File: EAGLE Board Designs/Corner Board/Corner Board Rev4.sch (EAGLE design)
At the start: 63 parts, among them J1 CONNECTOR-8_AMPHENOL_M12A_08P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, J2 CONNECTOR-2_MICROFIT_SMD_RIGH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, J3 BINDER-M12-A_4_PIN, J4 CONNECTOR-4_μF_S_RA_, T1 78613/3C_78613/3C_AIRGAP, U1 MAX7404, U10 LTC6820, U11 MCP3204, U2 OPAMP_1_CHANNEL_OPA991, U3 INA823DT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

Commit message: fixed voltage divider gain text
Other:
- note added: "0.666x gain"
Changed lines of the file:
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@@
 <wire x1="271.018" y1="207.772" x2="145.034" y2="208.026" width="0.1524" layer="97"/>
 <text x="147.828" y="203.962" size="1.778" layer="97" font="vector">RAE Tech SteeringTorque Sensor</text>
+<text x="187.198" y="168.402" size="1.27" layer="97" font="vector">0.666x gain</text>
 </plain>
 <instances>

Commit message: eagle is delayed
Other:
- note added: "0.67x gain"
- note removed: "0.666x gain"
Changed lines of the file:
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@@
 <wire x1="271.018" y1="207.772" x2="145.034" y2="208.026" width="0.1524" layer="97"/>
 <text x="147.828" y="203.962" size="1.778" layer="97" font="vector">RAE Tech SteeringTorque Sensor</text>
-<text x="187.198" y="168.402" size="1.27" layer="97" font="vector">0.666x gain</text>
+<text x="187.198" y="168.402" size="1.27" layer="97" font="vector">0.67x gain</text>
 </plain>
 <instances>

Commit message: small changes
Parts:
- added J5: CONNECTOR-4_μF_S_RA_, HyTechDevices:CONNECTOR-4_μF_S_RA_
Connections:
- net +24V: now also J5.1
- net GND: now also J5.4
- net STEER_TORQUE_24V: now also J5.3
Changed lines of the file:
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@@
 <part name="R7" library="HyTechDevices" deviceset="RESISTOR_?_*" device="0603" technology="10K"/>
 <part name="R8" library="HyTechDevices" deviceset="RESISTOR_?_*" device="0603" technology="20K"/>
+<part name="J5" library="HyTechDevices" deviceset="CONNECTOR-4_?_*" device="μF_S_RA" value="CONNECTOR-4_μF_S_RA_"/>
+<part name="P63" library="HyTechSupplies" deviceset="GND" device=""/>
+<part name="U$8" library="HyTechSupplies" deviceset="+24V" device=""/>
 </parts>
 <sheets>
@@
 <attribute name="VALUE" x="201.93" y="71.628" size="1.27" layer="96" align="bottom-center"/>
 </instance>
+<instance part="J5" gate="G$1" x="5.08" y="-42.418" smashed="yes">
+<attribute name="MPN" x="5.08" y="-55.753" size="1.27" layer="96" align="top-left"/>
+<attribute name="NAME" x="5.08" y="-41.656" size="1.27" layer="95"/>
+</instance>
+<instance part="P63" gate="1" x="17.78" y="-57.658" smashed="yes">
+<attribute name="VALUE" x="17.78" y="-58.928" size="1.27" layer="96" align="top-center"/>
+</instance>
+<instance part="U$8" gate="G$1" x="17.78" y="-39.878" smashed="yes">
+<attribute name="VALUE" x="17.78" y="-34.798" size="1.778" layer="96" align="bottom-center"/>
+</instance>
 </instances>
 <busses>
@@
 <pinref part="P12" gate="1" pin="GND"/>
 </segment>
+<segment>
+<pinref part="J5" gate="G$1" pin="4"/>
+<pinref part="P63" gate="1" pin="GND"/>
+<wire x1="15.24" y1="-52.578" x2="17.78" y2="-52.578" width="0.1524" layer="91"/>
+<wire x1="17.78" y1="-52.578" x2="17.78" y2="-55.118" width="0.1524" layer="91"/>
+</segment>
 </net>
 <net name="SIGNAL_P" class="0">
@@
 <junction x="73.66" y="63.5"/>
 </segment>
+<segment>
+<pinref part="U$8" gate="G$1" pin="+24V"/>
+<wire x1="17.78" y1="-44.958" x2="17.78" y2="-42.418" width="0.1524" layer="91"/>
+<pinref part="J5" gate="G$1" pin="1"/>
+<wire x1="17.78" y1="-44.958" x2="15.24" y2="-44.958" width="0.1524" layer="91"/>
+</segment>
 </net>
 <net name="SUS_POT_1" class="0">
@@
 </segment>
 </net>
+<net name="STEER_TORQUE_24V" class="0">
+<segment>
+<pinref part="J5" gate="G$1" pin="3"/>
+<wire x1="15.24" y1="-50.038" x2="18.288" y2="-50.038" width="0.1524" layer="91"/>
+<label x="18.288" y="-50.038" size="1.27" layer="95" font="vector" xref="yes"/>
+</segment>
+</net>

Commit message: did some routing
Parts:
- C2: value CAPACITOR_0603_25V_0.1UF -> CAPACITOR_0603_35V_0.1UF; device HyTechDevices:CAPACITOR_0603_25V_0.1UF -> HyTechDevices:CAPACITOR_0603_35V_0.1UF
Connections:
- net +24V: now also C2.1, U3P.VDD
- net +3V3: no longer C2.1, U3P.VDD
- net LOAD_CELL_FILTERED: now also U11.CH2; no longer U11.CH0
- net STEER_TORQUE_FILTERED: now also U11.CH0
- net SUS_POT_FILTERED: now also U11.CH1; no longer U11.CH2
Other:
- moved on the sheet: U11

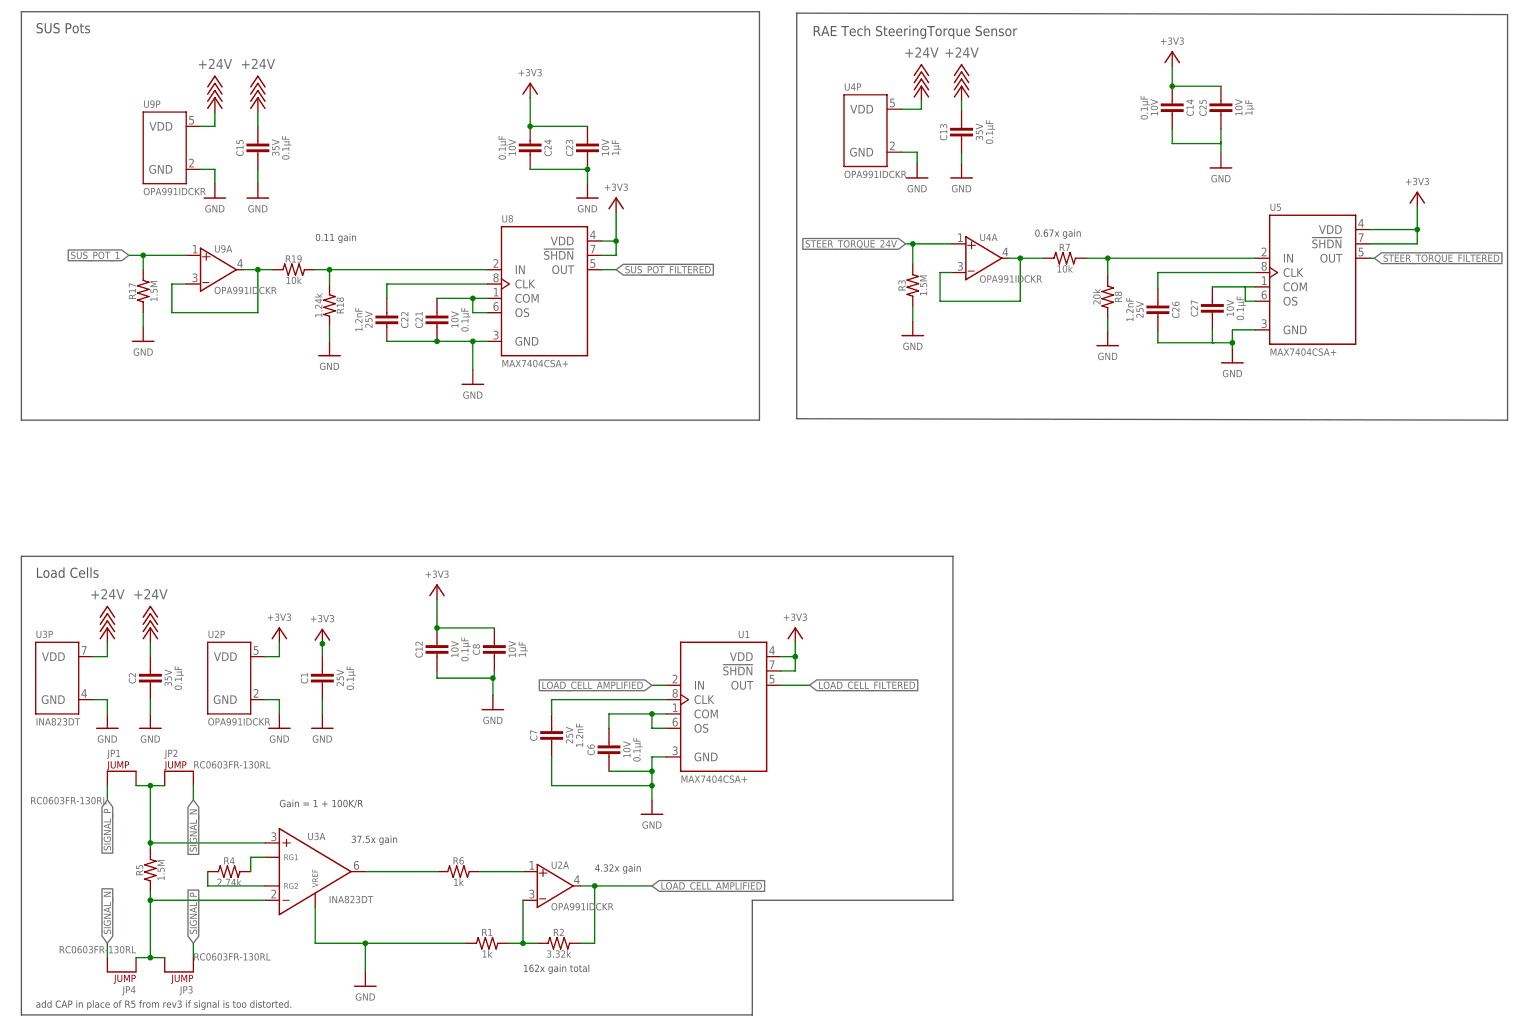
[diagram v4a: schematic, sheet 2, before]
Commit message: changed non crit for 2nd order
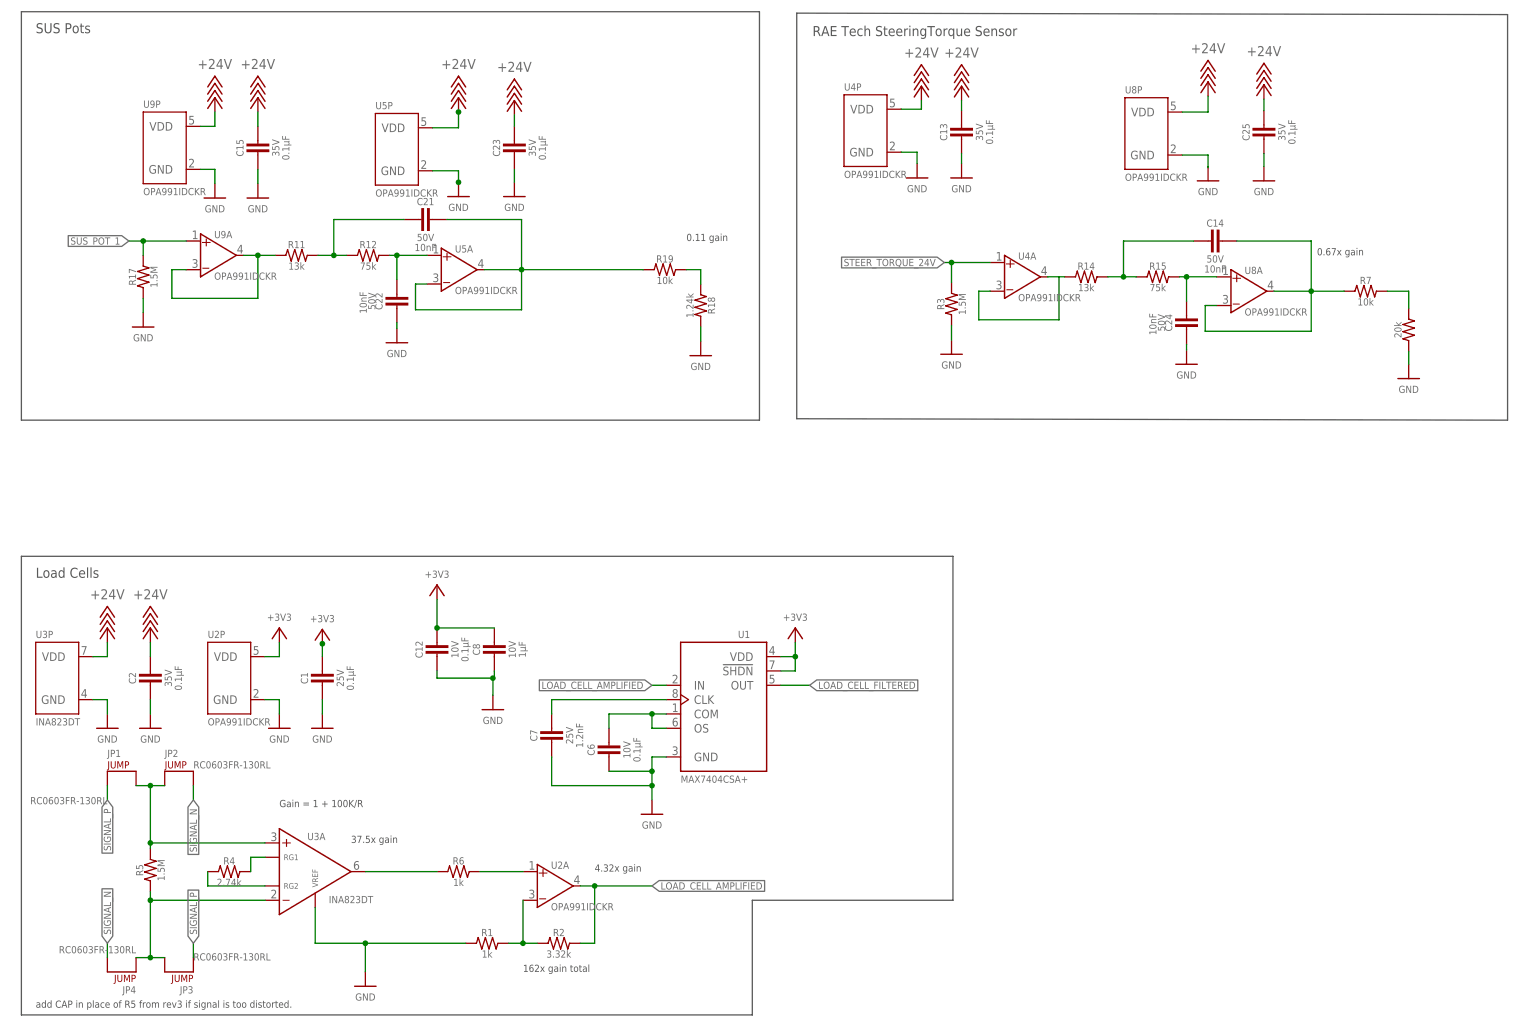
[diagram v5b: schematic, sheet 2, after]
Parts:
- removed C26: CAPACITOR_0603_25V_1.2NF, HyTechDevices:CAPACITOR_0603_25V_1.2NF
- removed C27: CAPACITOR_0603_10V_0.1UF, HyTechDevices:CAPACITOR_0603_10V_0.1UF
- added R11, R14: RESISTOR_0603_13K, HyTechDevices:RESISTOR_0603_13K
- added R12, R15: RESISTOR_0603_75K, HyTechDevices:RESISTOR_0603_75K
- C14, C21, C24: value CAPACITOR_0603_10V_0.1UF -> CAPACITOR_0603_50V_10NF; device HyTechDevices:CAPACITOR_0603_10V_0.1UF -> HyTechDevices:CAPACITOR_0603_50V_10NF
- C22: value CAPACITOR_0603_25V_1.2NF -> CAPACITOR_0603_50V_10NF; device HyTechDevices:CAPACITOR_0603_25V_1.2NF -> HyTechDevices:CAPACITOR_0603_50V_10NF
- C23, C25: value CAPACITOR_0603_10V_1UF -> CAPACITOR_0603_35V_0.1UF; device HyTechDevices:CAPACITOR_0603_10V_1UF -> HyTechDevices:CAPACITOR_0603_35V_0.1UF
- U5, U8: value MAX7404 -> OPAMP_1_CHANNEL_OPA991; device HyTechDevices:MAX7404 -> HyTechDevices:OPAMP_1_CHANNEL_OPA991
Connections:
- new net N$49: C22.1, R12.2, U5A.VIN+
- new net N$52: C24.1, R15.2, U8A.VIN+
- new net N$55: R7.1
- net +24V: now also C23.1, C25.1, U5P.VDD, U8P.VDD
- net +3V3: no longer C14.2, C23.1, C24.2, C25.1, U5.!SHDN, U5.VDD, U8.!SHDN, U8.VDD
- net GND: now also C22.2, C24.2, U5P.GND, U8P.GND; no longer C14.1, C21.2, C22.1, C24.1, C26.1, C27.2, U5.GND, U8.GND
- net N$15: now also C14.1, U8A.VIN-, U8A.VOUT; no longer C21.1, U8.COM, U8.OS
- net N$22: now also C21.1, R19.1, U5A.VIN-, U5A.VOUT; no longer C22.2, U8.CLK
- net N$51: now also R14.1; no longer R7.1
- net N$53: now also C21.2, R11.2, R12.1; no longer C27.1, U5.COM, U5.OS
- net N$54: now also C14.2, R14.2, R15.1; no longer C26.2, U5.CLK
- net STEER_TORQUE_3V3: no longer U5.IN
- net STEER_TORQUE_FILTERED: no longer U5.OUT
- net SUS_POT_1_24V1: now also R11.1; no longer R19.1
- net SUS_POT_1_3V3: no longer U8.IN
- net SUS_POT_FILTERED: no longer U8.OUT
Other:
- moved on the sheet: C14, C21, C22, C23, C24, C25, R17, R18, R19, R3, R7, U4A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

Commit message: redid everything
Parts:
- removed C13, C25: CAPACITOR_0603_35V_0.1UF, HyTechDevices:CAPACITOR_0603_35V_0.1UF
- removed C14, C24: CAPACITOR_0603_50V_10NF, HyTechDevices:CAPACITOR_0603_50V_10NF
- removed J5: CONNECTOR-4_μF_S_RA_, HyTechDevices:CONNECTOR-4_μF_S_RA_
- removed R14: RESISTOR_0603_13K, HyTechDevices:RESISTOR_0603_13K
- removed R15: RESISTOR_0603_75K, HyTechDevices:RESISTOR_0603_75K
- removed R3: RESISTOR_0603_1.5M, HyTechDevices:RESISTOR_0603_1.5M
- removed R7: RESISTOR_0603_10K, HyTechDevices:RESISTOR_0603_10K
- removed R8: RESISTOR_0603_20K, HyTechDevices:RESISTOR_0603_20K
- removed U4, U8: OPAMP_1_CHANNEL_OPA991, HyTechDevices:OPAMP_1_CHANNEL_OPA991
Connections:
- removed net N$15: C14.1, U8A.VIN-, U8A.VOUT
- removed net N$51: R14.1, U4A.VIN-, U4A.VOUT
- removed net N$52: C24.1, R15.2, U8A.VIN+
- removed net N$54: C14.2, R14.2, R15.1
- removed net N$55: R7.1
- removed net STEER_TORQUE_24V: J5.3, R3.2, U4A.VIN+
- removed net STEER_TORQUE_3V3: R7.2, R8.1
- removed net STEER_TORQUE_FILTERED: U11.CH0
- net +24V: no longer C13.1, C25.1, J5.1, U4P.VDD, U8P.VDD
- net DIFF_N: now also J1.6; no longer J1.4
- net DIFF_P: now also J1.5; no longer J1.3
- net GND: no longer C13.2, C24.2, C25.2, J5.4, R3.1, R8.2, U4P.GND, U8P.GND
- net POSTINTERLOCK: now also J1.4; no longer J1.6
- net PREINTERLOCK: now also J1.3; no longer J1.5
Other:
- note removed: "0.67x gain"
- note removed: "RAE Tech SteeringTorque Sensor"

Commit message: almost done
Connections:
- removed net SUS_POT_FILTERED: U11.CH1
- net SUS_POT_1_3V3: now also U11.CH1
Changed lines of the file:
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@@
 </segment>
 </net>
-<net name="SUS_POT_FILTERED" class="0">
+<net name="SUS_POT_1_3V3" class="0">
 <segment>
 <pinref part="U11" gate="G$1" pin="CH1"/>

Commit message: finito
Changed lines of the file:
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@@
-</segment>
-</net>
-<net name="LOAD_CELL_FILTERED" class="0">
-<segment>
-<pinref part="U1" gate="G$1" pin="OUT"/>
-<wire x1="142.24" y1="88.9" x2="147.32" y2="88.9" width="0.1524" layer="91"/>
-<label x="147.32" y="88.9" size="1.27" layer="95" font="vector" xref="yes"/>
 </segment>
 </net>
@@
 </segment>
 </net>
+<net name="LOAD_CELL_FILTERED" class="0">
+<segment>
+<pinref part="U1" gate="G$1" pin="OUT"/>
+<wire x1="142.24" y1="88.9" x2="145.034" y2="88.9" width="0.1524" layer="91"/>
+<label x="145.034" y="88.9" size="1.27" layer="95" font="vector" xref="yes"/>
+</segment>
+</net>
